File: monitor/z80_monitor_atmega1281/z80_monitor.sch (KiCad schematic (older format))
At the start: 2 parts, among them J1 Conn_02x25_Odd_Even, U1 ATmega1281-16AU

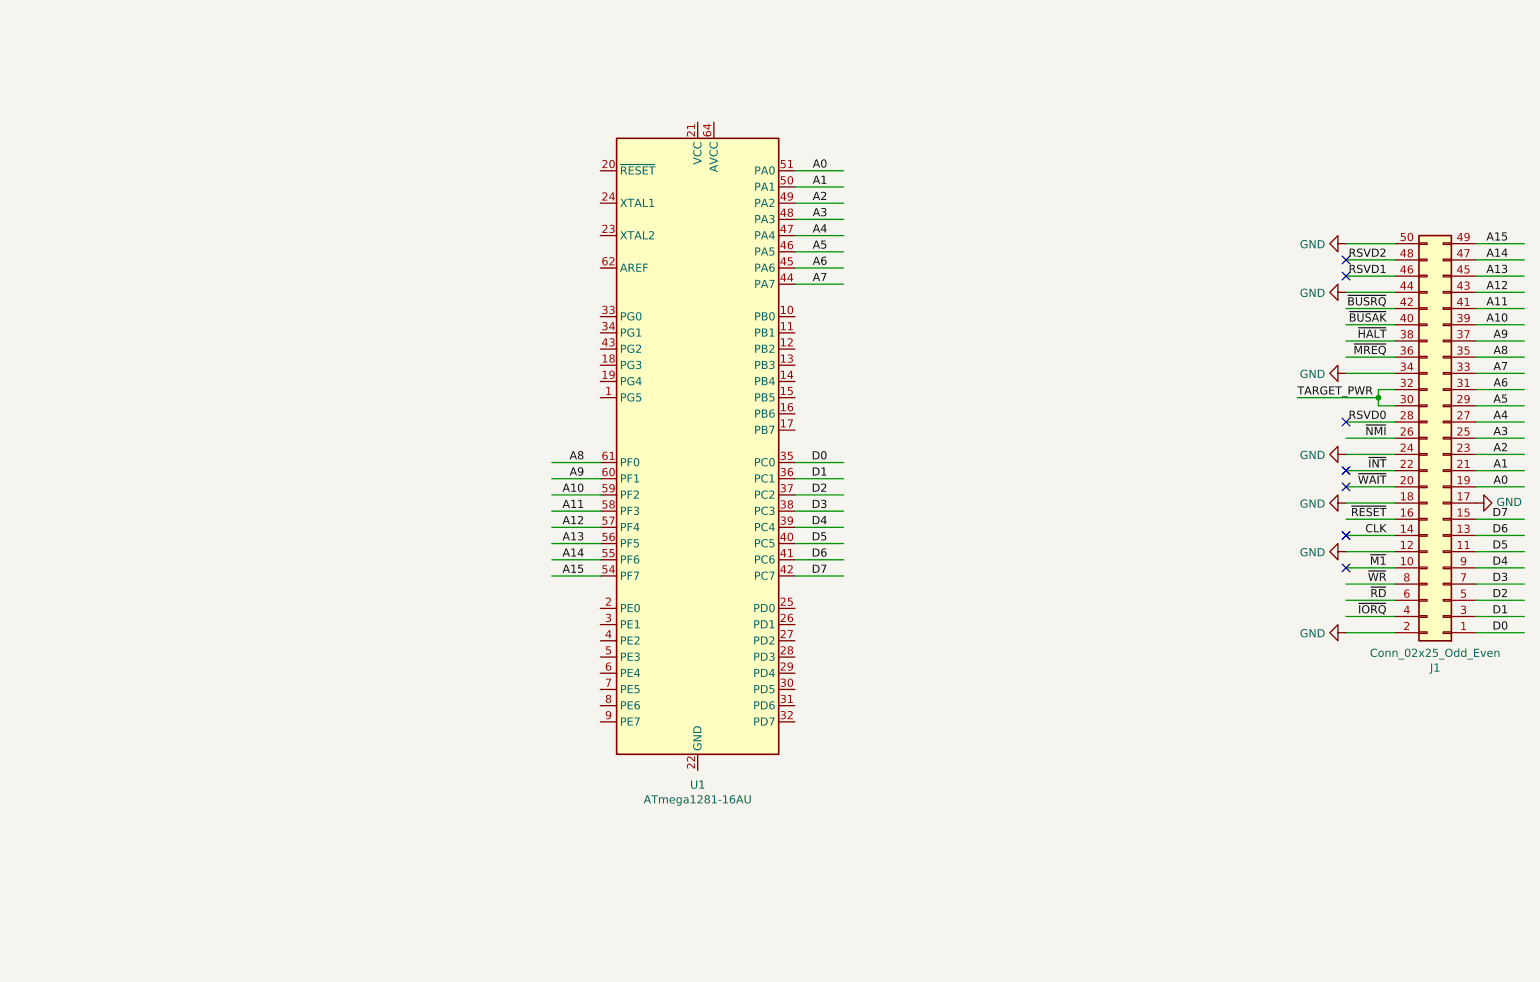
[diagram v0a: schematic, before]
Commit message: Finished new AVR-based monitor board, pending final checks and gerber generation.
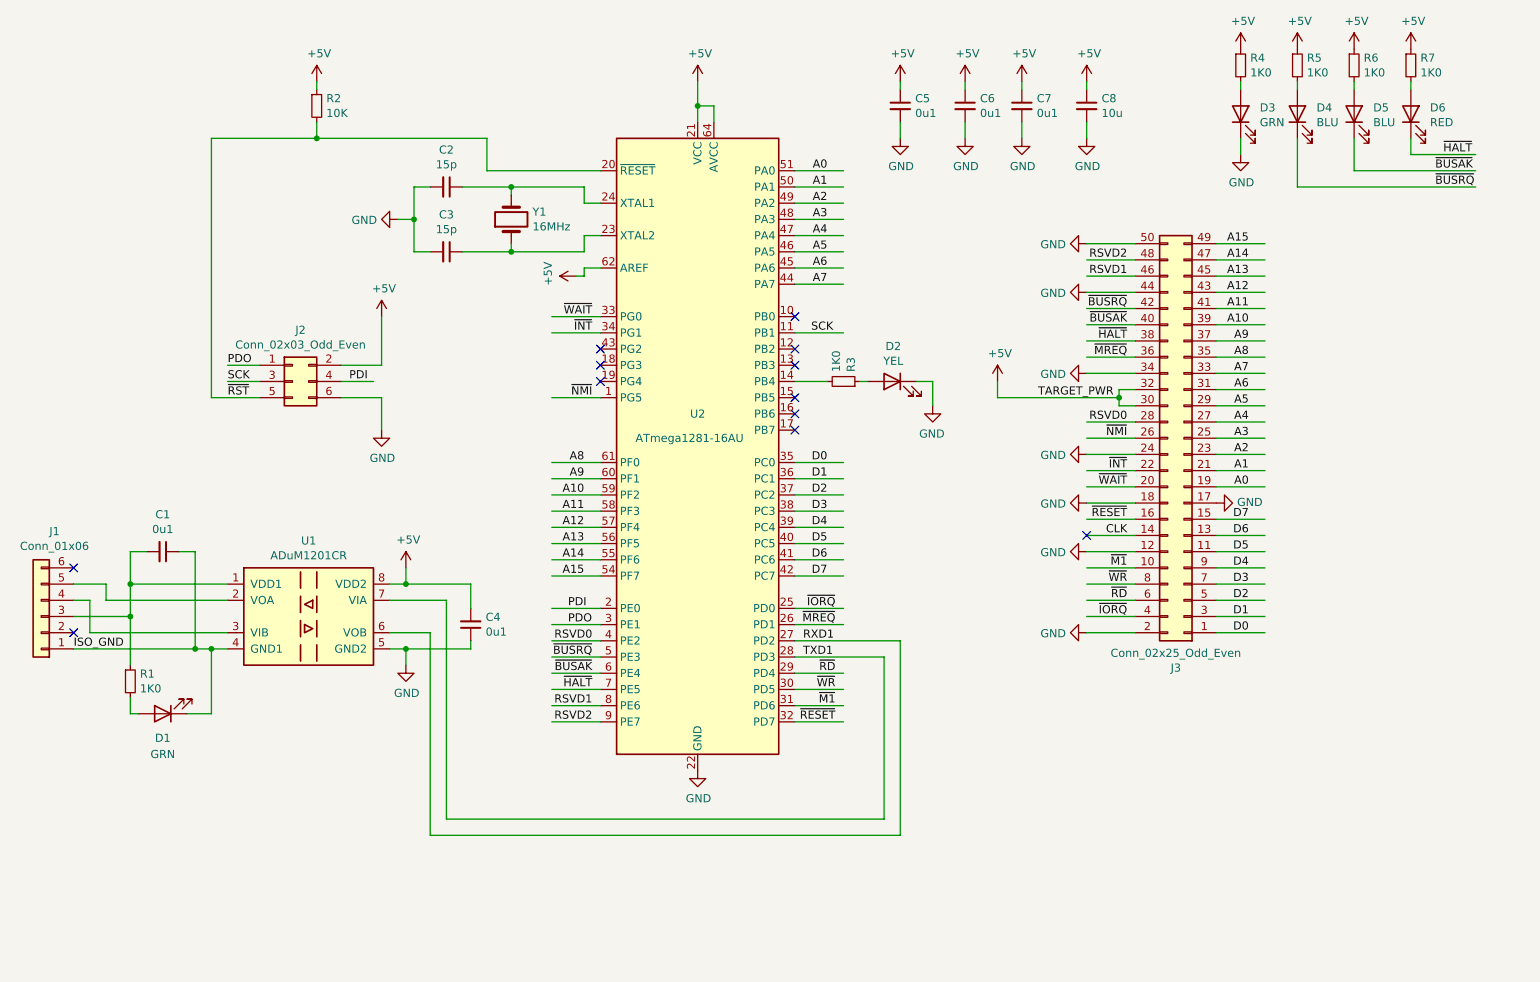
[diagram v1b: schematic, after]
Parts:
- added C1, C4, C5, C6, C7: 0u1, Capacitor_SMD:C_0603_1608Metric_Pad1.05x0.95mm_HandSolder, symbol Device:C_Small
- added C2, C3: 15p, Capacitor_SMD:C_0603_1608Metric_Pad1.05x0.95mm_HandSolder, symbol Device:C_Small
- added C8: 10u, Capacitor_SMD:C_1206_3216Metric_Pad1.42x1.75mm_HandSolder, symbol Device:C_Small
- added D1, D3: GRN, LED_SMD:LED_0603_1608Metric_Pad1.05x0.95mm_HandSolder, symbol Device:LED
- added D2: YEL, LED_SMD:LED_0603_1608Metric_Pad1.05x0.95mm_HandSolder, symbol Device:LED
- added D4, D5: BLU, LED_SMD:LED_0603_1608Metric_Pad1.05x0.95mm_HandSolder, symbol Device:LED
- added D6: RED, LED_SMD:LED_0603_1608Metric_Pad1.05x0.95mm_HandSolder, symbol Device:LED
- added J1: Conn_01x06, Connector_PinHeader_2.54mm:PinHeader_1x06_P2.54mm_Vertical, symbol Connector_Generic:Conn_01x06
- added J2: Conn_02x03_Odd_Even, Connector_PinHeader_2.54mm:PinHeader_2x03_P2.54mm_Vertical, symbol Connector_Generic:Conn_02x03_Odd_Even
- added R1, R3, R4, R5, R6, R7: 1K0, Resistor_SMD:R_0603_1608Metric_Pad1.05x0.95mm_HandSolder, symbol Device:R_Small
- added R2: 10K, Resistor_SMD:R_0603_1608Metric_Pad1.05x0.95mm_HandSolder, symbol Device:R_Small
- added U1: ADuM1201CR, Package_SO:SOIC-8_3.9x4.9mm_P1.27mm, symbol Isolator:ADuM1201CR
- added Y1: 16MHz, Crystal:Crystal_SMD_Abracon_ABM3-2Pin_5.0x3.2mm_HandSoldering, symbol Device:Crystal
- J3: renamed from J1; footprint Pin_Headers:Pin_Header_Straight_2x25_Pitch2.54mm -> Connector_IDC:IDC-Header_2x25_P2.54mm_Vertical
- U2: renamed from U1; Farnell (none) -> 1455092
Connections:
- net labels added: +5V, ISO_GND, PDI, PDO, RXD1, SCK, TXD1, ~RST~
- wire segments 76 -> 194
- no-connect marks 7 -> 12
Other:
- moved on the sheet: J3

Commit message: Various updates to board.
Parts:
- added C2: 100p, Capacitor_SMD:C_0603_1608Metric_Pad1.05x0.95mm_HandSolder, symbol Device:C_Small
- added H1: M2.5, MountingHole:MountingHole_2.7mm_M2.5_Pad_Via, symbol Mechanical:MountingHole_Pad
- added H2: MountingHole_Pad, MountingHole:MountingHole_2.7mm_M2.5_Pad_Via, symbol Mechanical:MountingHole_Pad
- renumbered C2 to C3, C3 to C4, C4 to C5, C5 to C6, C6 to C7, C7 to C8, C8 to C9
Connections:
- wire segments 194 -> 198
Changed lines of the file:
@@
 	4900 4000 4600 4000
 $Comp
-L power:GND #PWR010
+L power:GND #PWR09
 U 1 1 5FC9AFFA
 P 5500 5900
-F 0 "#PWR010" H 5500 5650 50  0001 C CNN
+F 0 "#PWR09" H 5500 5650 50  0001 C CNN
 F 1 "GND" H 5505 5727 50  0000 C CNN
 F 2 "" H 5500 5900 50  0001 C CNN
@@
 $EndComp
 $Comp
-L power:+5V #PWR09
+L power:+5V #PWR08
 U 1 1 5FC9BEF8
 P 5500 1650
-F 0 "#PWR09" H 5500 1500 50  0001 C CNN
+F 0 "#PWR08" H 5500 1500 50  0001 C CNN
 F 1 "+5V" H 5515 1823 50  0000 C CNN
 F 2 "" H 5500 1650 50  0001 C CNN
@@
 	4350 2700 4350 2650
 $Comp
-L Device:C_Small C2
+L Device:C_Small C3
 U 1 1 5FCAECC6
 P 3950 2300
-F 0 "C2" V 3721 2300 50  0000 C CNN
+F 0 "C3" V 3721 2300 50  0000 C CNN
 F 1 "15p" V 3812 2300 50  0000 C CNN
 F 2 "Capacitor_SMD:C_0603_1608Metric_Pad1.05x0.95mm_HandSolder" H 3950 2300 50  0001 C CNN
@@
 $EndComp
 $Comp
-L Device:C_Small C3
+L Device:C_Small C4
 U 1 1 5FCAF8D1
 P 3950 2700
-F 0 "C3" V 3721 2700 50  0000 C CNN
+F 0 "C4" V 3721 2700 50  0000 C CNN
 F 1 "15p" V 3812 2700 50  0000 C CNN
 F 2 "Capacitor_SMD:C_0603_1608Metric_Pad1.05x0.95mm_HandSolder" H 3950 2700 50  0001 C CNN
@@
 	3750 2500 3750 2700
 $Comp
-L Device:C_Small C5
+L Device:C_Small C6
 U 1 1 5FCC8FBB
 P 6750 1800
-F 0 "C5" H 6842 1846 50  0000 L CNN
+F 0 "C6" H 6842 1846 50  0000 L CNN
 F 1 "0u1" H 6842 1755 50  0000 L CNN
 F 2 "Capacitor_SMD:C_0603_1608Metric_Pad1.05x0.95mm_HandSolder" H 6750 1800 50  0001 C CNN
@@
 $EndComp
 $Comp
-L power:+5V #PWR011
+L power:+5V #PWR010
 U 1 1 5FCCA6C7
 P 6750 1650
-F 0 "#PWR011" H 6750 1500 50  0001 C CNN
+F 0 "#PWR010" H 6750 1500 50  0001 C CNN
 F 1 "+5V" H 6765 1823 50  0000 C CNN
 F 2 "" H 6750 1650 50  0001 C CNN
@@
 	6750 1700 6750 1650
 $Comp
-L power:GND #PWR012
+L power:GND #PWR011
 U 1 1 5FCCFE5D
 P 6750 2000
-F 0 "#PWR012" H 6750 1750 50  0001 C CNN
+F 0 "#PWR011" H 6750 1750 50  0001 C CNN
 F 1 "GND" H 6755 1827 50  0000 C CNN
 F 2 "" H 6750 2000 50  0001 C CNN
@@
 PDO
 $Comp
-L power:+5V #PWR08
+L power:+5V #PWR07
 U 1 1 5FF2E6AC
 P 4750 2850
-F 0 "#PWR08" H 4750 2700 50  0001 C CNN
+F 0 "#PWR07" H 4750 2700 50  0001 C CNN
 F 1 "+5V" H 4765 3023 50  0000 C CNN
 F 2 "" H 4750 2850 50  0001 C CNN
@@
 	4800 2850 4750 2850
 $Comp
-L Device:C_Small C6
+L Device:C_Small C7
 U 1 1 5FF77B41
 P 7150 1800
-F 0 "C6" H 7242 1846 50  0000 L CNN
+F 0 "C7" H 7242 1846 50  0000 L CNN
 F 1 "0u1" H 7242 1755 50  0000 L CNN
 F 2 "Capacitor_SMD:C_0603_1608Metric_Pad1.05x0.95mm_HandSolder" H 7150 1800 50  0001 C CNN
@@
 	7150 2000 7150 1900
 $Comp
-L Device:C_Small C8
+L Device:C_Small C9
 U 1 1 5FFA94C2
 P 7900 1800
-F 0 "C8" H 7992 1846 50  0000 L CNN
+F 0 "C9" H 7992 1846 50  0000 L CNN
 F 1 "10u" H 7992 1755 50  0000 L CNN
 F 2 "Capacitor_SMD:C_1206_3216Metric_Pad1.42x1.75mm_HandSolder" H 7900 1800 50  0001 C CNN
@@
 L power:+5V #PWR05
 U 1 1 5FCDAA4C
-P 3700 4650
-F 0 "#PWR05" H 3700 4500 50  0001 C CNN
-F 1 "+5V" H 3715 4823 50  0000 C CNN
-F 2 "" H 3700 4650 50  0001 C CNN
-F 3 "" H 3700 4650 50  0001 C CNN
-	1    3700 4650
+P 4100 4650
+F 0 "#PWR05" H 4100 4500 50  0001 C CNN
+F 1 "+5V" H 4115 4823 50  0000 C CNN
+F 2 "" H 4100 4650 50  0001 C CNN
+F 3 "" H 4100 4650 50  0001 C CNN
+	1    4100 4650
 	1    0    0    -1
 $EndComp
@@
 L power:GND #PWR06
 U 1 1 5FCE3E63
-P 3700 5250
-F 0 "#PWR06" H 3700 5000 50  0001 C CNN
-F 1 "GND" H 3705 5077 50  0000 C CNN
-F 2 "" H 3700 5250 50  0001 C CNN
-F 3 "" H 3700 5250 50  0001 C CNN
-	1    3700 5250
-	1    0    0    -1
-$EndComp
-Wire Wire Line
-	3600 4750 3700 4750
-Wire Wire Line
-	3700 4750 3700 4650
-Wire Wire Line
-	3600 5150 3700 5150
-Wire Wire Line
-	3700 5150 3700 5250
+P 4100 5250
+F 0 "#PWR06" H 4100 5000 50  0001 C CNN
+F 1 "GND" H 4105 5077 50  0000 C CNN
+F 2 "" H 4100 5250 50  0001 C CNN
+F 3 "" H 4100 5250 50  0001 C CNN
+	1    4100 5250
+	1    0    0    -1
+$EndComp
+Wire Wire Line
+	3600 4750 4100 4750
+Wire Wire Line
+	4100 4750 4100 4650
+Wire Wire Line
+	3600 5150 3650 5150
+Wire Wire Line
+	4100 5150 4100 5250
 Wire Wire Line
 	3600 5050 3850 5050
@@
 $EndComp
 Wire Wire Line
-	2600 5150 2500 5150
+	2600 5150 2550 5150
 Wire Wire Line
 	2600 4750 2000 4750
@@
 	2400 5150 1650 5150
 Wire Wire Line
-	2350 5550 2500 5550
-Wire Wire Line
-	2500 5550 2500 5150
-Connection ~ 2500 5150
-Wire Wire Line
-	2500 5150 2400 5150
+	2350 5550 2450 5550
+Wire Wire Line
+	2450 5550 2450 5150
+Connection ~ 2450 5150
+Wire Wire Line
+	2450 5150 2400 5150
 Wire Wire Line
 	2050 5550 2000 5550
@@
 	6500 3500 6550 3500
 $Comp
-L power:GND #PWR07
+L power:GND #PWR012
 U 1 1 5FF3FD2B
 P 6950 3650
-F 0 "#PWR07" H 6950 3400 50  0001 C CNN
+F 0 "#PWR012" H 6950 3400 50  0001 C CNN
 F 1 "GND" H 6955 3477 50  0000 C CNN
 F 2 "" H 6950 3650 50  0001 C CNN
@@
 	9550 2200 10300 2200
 $Comp
-L Device:C_Small C4
+L Device:C_Small C5
 U 1 1 5FFB5E05
 P 4100 5000
-F 0 "C4" H 4008 4954 50  0000 R CNN
+F 0 "C5" H 4008 4954 50  0000 R CNN
 F 1 "0u1" H 4008 5045 50  0000 R CNN
 F 2 "Capacitor_SMD:C_0603_1608Metric_Pad1.05x0.95mm_HandSolder" H 4100 5000 50  0001 C CNN
@@
 $EndComp
 Wire Wire Line
-	3700 4750 4100 4750
-Wire Wire Line
 	4100 4750 4100 4900
-Connection ~ 3700 4750
-Wire Wire Line
-	3700 5150 4100 5150
+Connection ~ 4100 4750
 Wire Wire Line
 	4100 5150 4100 5100
-Connection ~ 3700 5150
-$Comp
-L Device:C_Small C7
+Connection ~ 4100 5150
+$Comp
+L Device:C_Small C8
 U 1 1 60087769
 P 7500 1800
-F 0 "C7" H 7592 1846 50  0000 L CNN
+F 0 "C8" H 7592 1846 50  0000 L CNN
 F 1 "0u1" H 7592 1755 50  0000 L CNN
 F 2 "Capacitor_SMD:C_0603_1608Metric_Pad1.05x0.95mm_HandSolder" H 7500 1800 50  0001 C CNN
@@
 NoConn ~ 1650 5050
 NoConn ~ 1650 4650
+$Comp
+L Device:C_Small C2
+U 1 1 5FCF19FE
+P 3100 5550
+F 0 "C2" H 3008 5504 50  0000 R CNN
+F 1 "100p" H 3008 5595 50  0000 R CNN
+F 2 "Capacitor_SMD:C_0603_1608Metric_Pad1.05x0.95mm_HandSolder" H 3100 5550 50  0001 C CNN
+F 3 "~" H 3100 5550 50  0001 C CNN
+	1    3100 5550
+	0    -1   -1   0
+$EndComp
+Wire Wire Line
+	3000 5550 2550 5550
+Wire Wire Line
+	2550 5550 2550 5150
+Connection ~ 2550 5150
+Wire Wire Line
+	2550 5150 2450 5150
+Wire Wire Line
+	3200 5550 3650 5550
+Wire Wire Line
+	3650 5550 3650 5150
+Connection ~ 3650 5150
+Wire Wire Line
+	3650 5150 4100 5150
+$Comp
+L Mechanical:MountingHole_Pad H1
+U 1 1 5FD5DC17
+P 4200 6800
+F 0 "H1" H 4300 6849 50  0000 L CNN
+F 1 "M2.5" H 4300 6758 50  0000 L CNN
+F 2 "MountingHole:MountingHole_2.7mm_M2.5_Pad_Via" H 4200 6800 50  0001 C CNN
+F 3 "~" H 4200 6800 50  0001 C CNN
+	1    4200 6800
+	1    0    0    -1
+$EndComp
+$Comp
+L power:GND #PWR0101
+U 1 1 5FD5F15E
+P 4200 6900
+F 0 "#PWR0101" H 4200 6650 50  0001 C CNN
+F 1 "GND" H 4205 6727 50  0000 C CNN
+F 2 "" H 4200 6900 50  0001 C CNN
+F 3 "" H 4200 6900 50  0001 C CNN
+	1    4200 6900
+	1    0    0    -1
+$EndComp
+$Comp
+L power:GND #PWR033
+U 1 1 5FD9DEB6
+P 5200 6900
+F 0 "#PWR033" H 5200 6650 50  0001 C CNN
+F 1 "GND" H 5205 6727 50  0000 C CNN
+F 2 "" H 5200 6900 50  0001 C CNN
+F 3 "" H 5200 6900 50  0001 C CNN
+	1    5200 6900
+	1    0    0    -1
+$EndComp
+$Comp
+L Mechanical:MountingHole_Pad H2
+U 1 1 5FD9DEB0
+P 5200 6800
+F 0 "H2" H 5300 6849 50  0000 L CNN
+F 1 "MountingHole_Pad" H 5300 6758 50  0000 L CNN
+F 2 "MountingHole:MountingHole_2.7mm_M2.5_Pad_Via" H 5200 6800 50  0001 C CNN
+F 3 "~" H 5200 6800 50  0001 C CNN
+	1    5200 6800
+	1    0    0    -1
+$EndComp
 $EndSCHEMATC
